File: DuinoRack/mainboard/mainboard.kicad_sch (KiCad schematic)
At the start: 67 parts, among them J1 ISP, J2 SER, J3 Conn_02x08_Odd_Even, J4 Conn_02x05_Odd_Even, J5 Conn_MIDI, U1 MCP4822, U2 ATmega328P-P, U3 TL074, U4 TL431LP, U5 MCP6004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

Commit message: Add programming jumper, fix up MIDI in and THRU
We need to disconnect midi in during programming, since it will pull up
RX. Hence the new jumper.
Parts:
- added C18, C19, C20, C24, C25, C26: 100n, Capacitor_SMD:C_0603_1608Metric_Pad1.08x0.95mm_HandSolder, symbol Device:C
- added C21, C22, C23: 1n, Capacitor_SMD:C_0603_1608Metric_Pad1.08x0.95mm_HandSolder, symbol Device:C
- added H1: MountingHole, MountingHole:MountingHole_3.2mm_M3_DIN965, symbol Mechanical:MountingHole
- added JP1: !PROGRAM, Connector_PinHeader_2.54mm:PinHeader_1x02_P2.54mm_Vertical, symbol Jumper:Jumper_2_Open
- added R29, R36, R37: 220, Resistor_SMD:R_0603_1608Metric_Pad0.98x0.95mm_HandSolder, symbol Device:R
- added R38, R40: 18k, Resistor_SMD:R_0603_1608Metric_Pad0.98x0.95mm_HandSolder, symbol Device:R
- added R39: 4.7k, Resistor_SMD:R_0603_1608Metric_Pad0.98x0.95mm_HandSolder, symbol Device:R
- C2, C4: value C -> 100n
- D7: footprint Diode_SMD:D_SMA-SMB_Universal_Handsoldering -> Diode_SMD:D_SOD-523
- J5: footprint Connector_PinHeader_2.54mm:PinHeader_1x07_P2.54mm_Vertical -> Connector_PinHeader_2.54mm:PinHeader_1x06_P2.54mm_Vertical; symbol Connector:Conn_01x07_Male -> Connector:Conn_01x06_Male
- R27, R28: renamed from R?; footprint (none) -> Resistor_SMD:R_0603_1608Metric_Pad0.98x0.95mm_HandSolder
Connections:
- net +12V: now also C24.1
- net +5V: now also C26.1
- net -12V: now also C25.1
- net GND: now also J3.15 (Pin_15), C18.1, C19.1, C20.1, C22.2, C24.2, C25.2, C26.2, R39.2; no longer J5.1 (Pin_1)
- net MIDI_IN_4: now also J5.1 (Pin_1), R33.2; no longer J5.2 (Pin_2)
- net MIDI_IN_5: now also J5.2 (Pin_2); no longer J5.3 (Pin_3)
- net MIDI_OUT_4: now also J5.5 (Pin_5), R32.2; no longer J5.6 (Pin_6), R31.2
- net MIDI_OUT_5: now also J5.6 (Pin_6), R31.2; no longer J5.7 (Pin_7), R32.2
- net MIDI_THRU_4: now also J5.3 (Pin_3), R26.2; no longer J2.3 (Pin_3), J5.4 (Pin_4), R25.1, U2.2 (PD0), U7.6 (VO2)
- net MIDI_THRU_5: now also J5.4 (Pin_4), R25.1, U7.6 (VO2), JP1.2 (B); no longer J5.5 (Pin_5), R26.2
- net OUTB_INT: now also C23.2, R40.2
- net at U1.6 (VB): now also R29.1
- new net: C19.2, R36.2, R37.1
- new net: C20.2, C21.1, R37.2, R38.1
- new net: C22.1, R38.2, R40.1
- new net: C18.2, R29.2, R36.1
- new net: C21.2, C23.1, R39.1
- new net RX: J2.3 (Pin_3), JP1.1 (A), U2.2 (PD0)
- no-connect marks 3 -> 2
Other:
- note added: "solder jumpers to swap 4/5"
- note removed: "(IN3, inverted)"
- moved on the sheet: C10, C11, C12, C15, C5, C6, C8, C9, D7, R10, R11, R15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

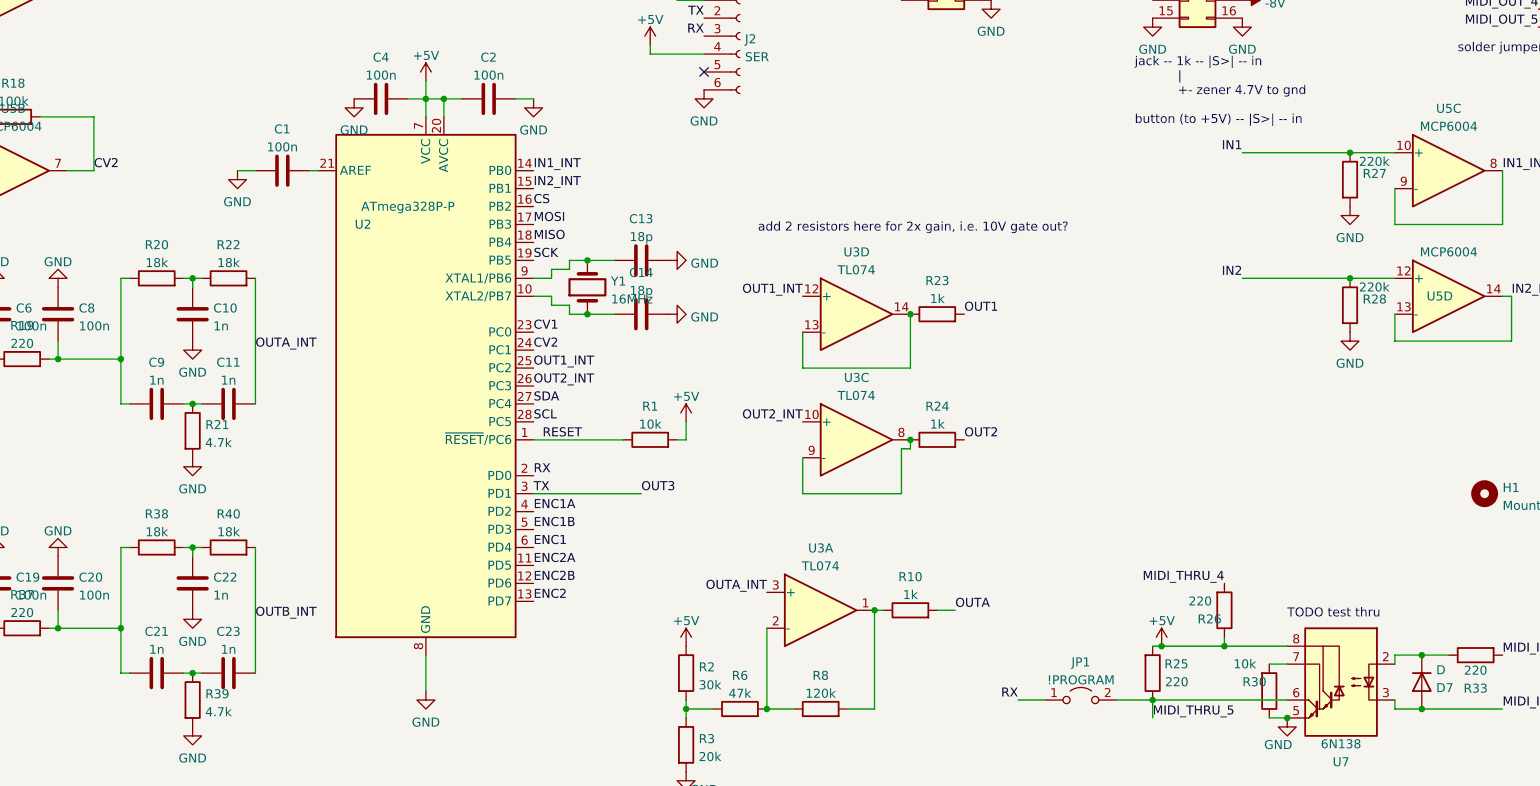
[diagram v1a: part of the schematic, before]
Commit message: Move gate outputs to Timer1 ports
By having the gate outputs connected to Timer1, we can drive them with
PWM, enabling up for other later use cases. A low-pass filter was added
in the output stage to accommodate for this.

We'll keep using normal digital I/O in gate mode, since PWM would be
too noisy there.
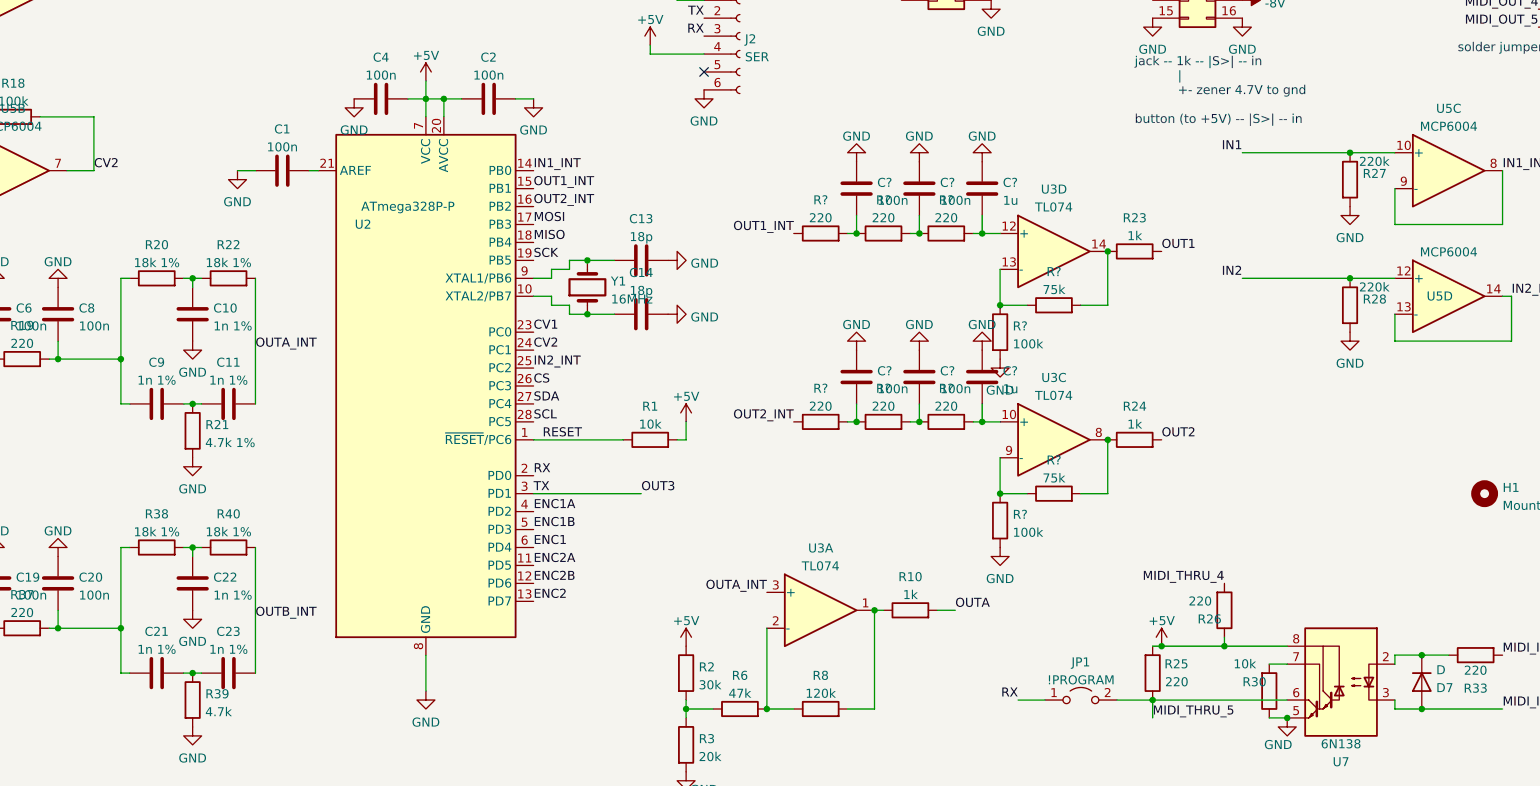
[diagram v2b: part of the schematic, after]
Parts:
- added C? (x4): 100n, Capacitor_SMD:C_0603_1608Metric_Pad1.08x0.95mm_HandSolder, symbol Device:C
- added C? (x2): 1u, Capacitor_SMD:C_0603_1608Metric_Pad1.08x0.95mm_HandSolder, symbol Device:C
- added R? (x2): 75k, symbol Device:R
- added R? (x6): 220, Resistor_SMD:R_0603_1608Metric_Pad0.98x0.95mm_HandSolder, symbol Device:R
- added R? (x2): 100k, symbol Device:R
- C10, C11, C21, C22, C23, C9: value 1n -> 1n 1%
- R20, R22, R38, R40: value 18k -> 18k 1%
- R21: value 4.7k -> 4.7k 1%
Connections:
- net CS: now also U2.26 (PC3); no longer U2.16 (PB2)
- net GND: now also C?.1, C?.1, C?.1, C?.1, C?.1, C?.1, R?.2, R?.2
- net IN2_INT: now also U2.25 (PC2); no longer U2.15 (PB1)
- net OUT1_INT: now also U2.15 (PB1), R?.1; no longer U2.25 (PC2), U3.12 (+)
- net OUT2_INT: now also U2.16 (PB2), R?.1; no longer U2.26 (PC3), U3.10 (+)
- net at R23.1, U3.14: now also R?.2; no longer U3.13 (-)
- net at R24.1, U3.8: now also R?.2; no longer U3.9 (-)
- new net: R?.1, R?.1, U3.13 (-)
- new net: C?.2, R?.1, R?.2 (x4)
- new net: C?.2, R?.2, U3.12 (+)
- new net: R?.1, R?.1, U3.9 (-)
- new net: C?.2, R?.2, U3.10 (+)
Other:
- note removed: "TODO test thru"
- note removed: "add 2 resistors here for 2x gain, i.e. 10V gate out?"
- moved on the sheet: R23, R24, U3C, U3D

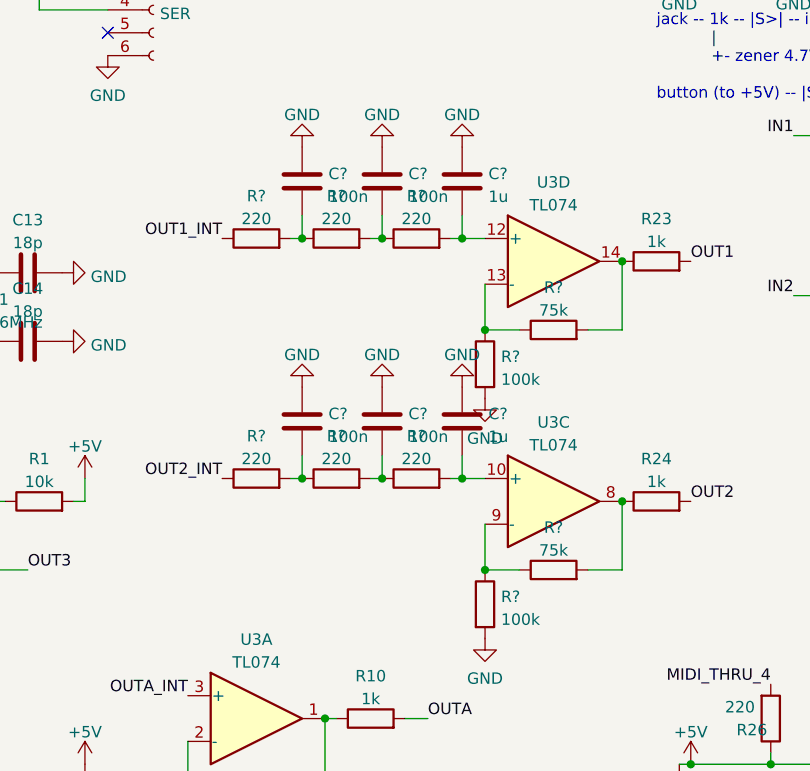
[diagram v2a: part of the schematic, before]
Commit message: Update layout with latest pcb changes
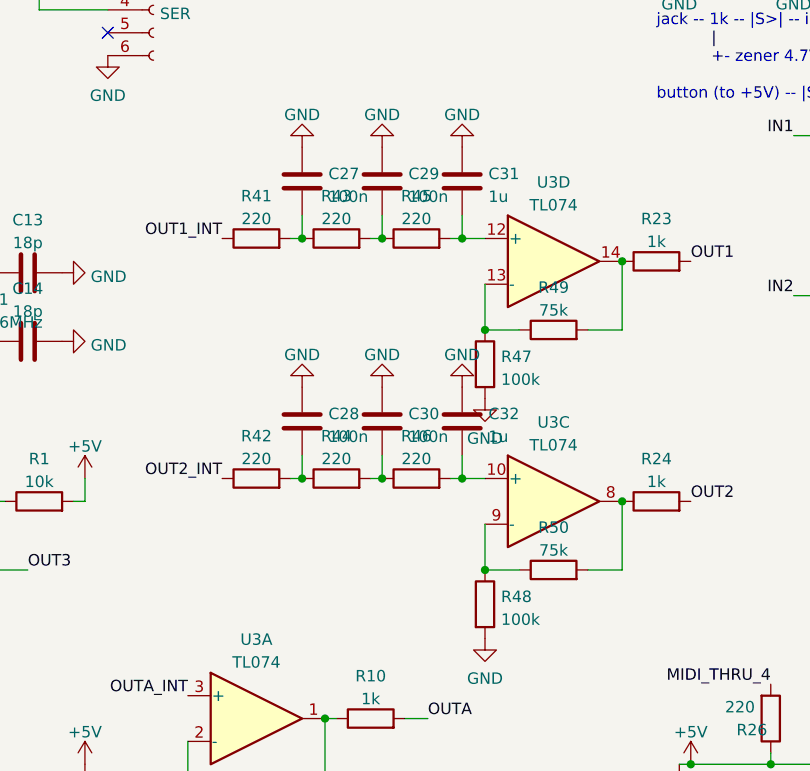
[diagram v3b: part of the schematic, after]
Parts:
- R47, R48, R49, R50: renamed from R?; footprint (none) -> Resistor_SMD:R_0603_1608Metric_Pad0.98x0.95mm_HandSolder
- gave numbers to parts that had none: 12

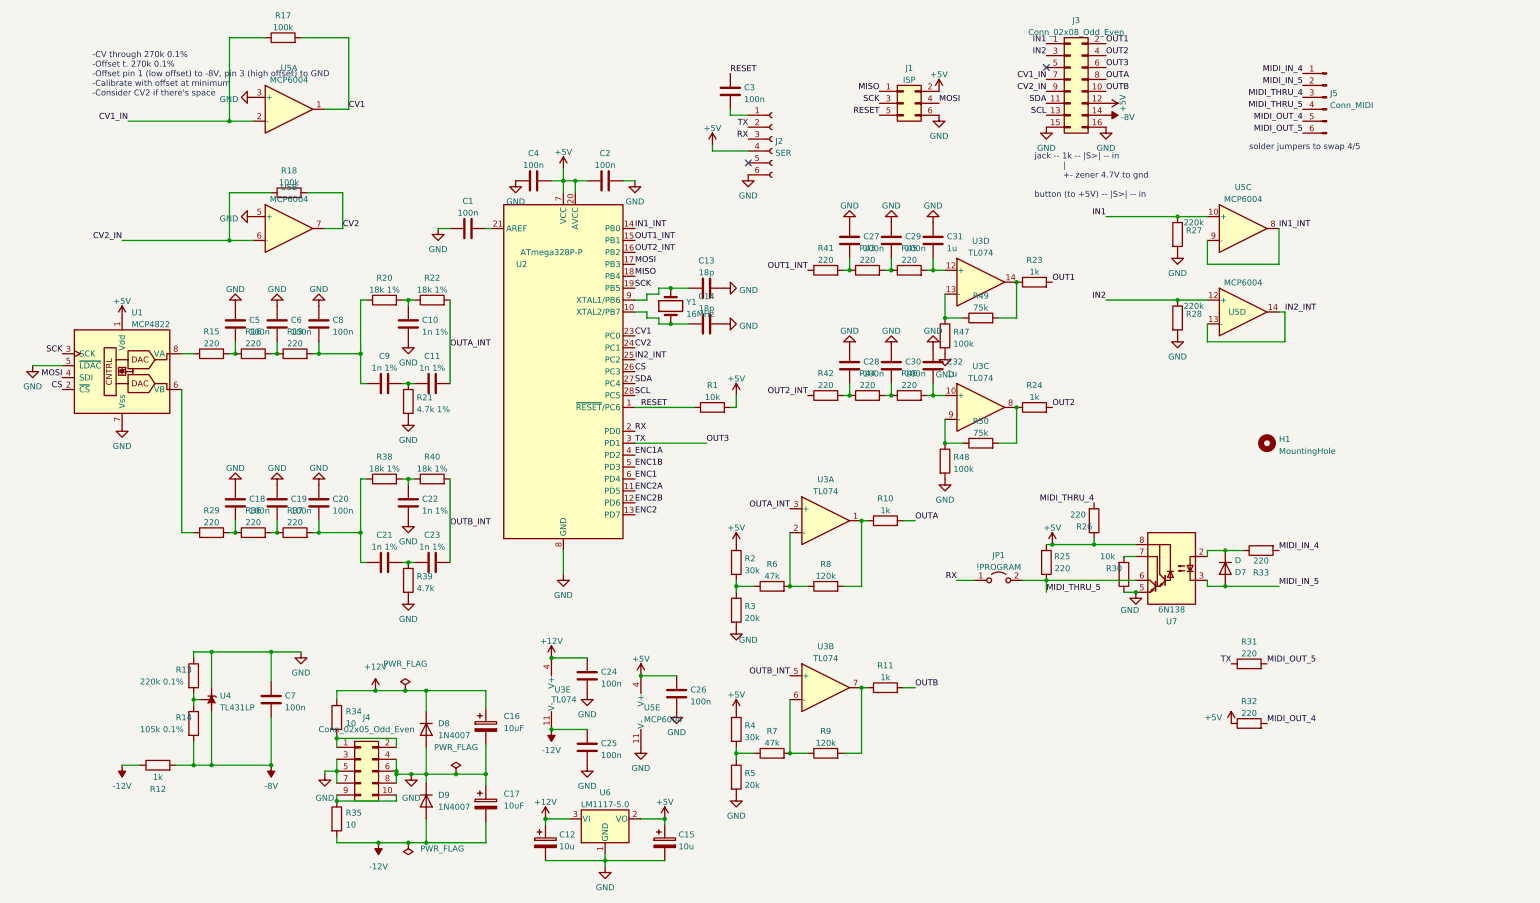
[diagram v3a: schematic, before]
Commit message: Add configurable input protection to enable gate IN3
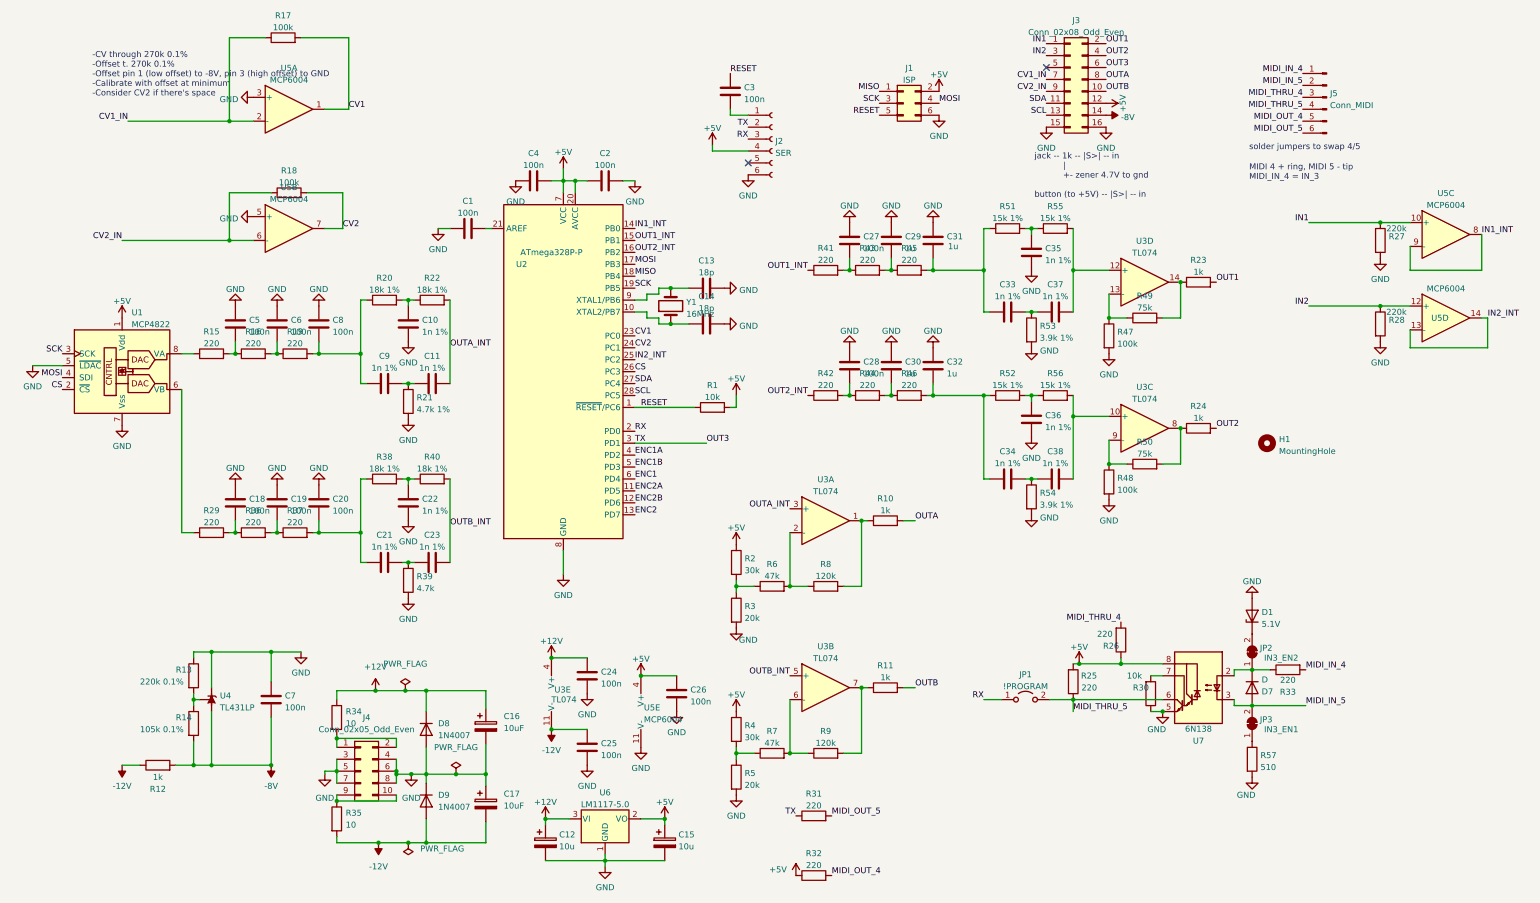
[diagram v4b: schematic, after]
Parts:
- added C33, C34, C35, C36, C37, C38: 1n 1%, Capacitor_SMD:C_0603_1608Metric_Pad1.08x0.95mm_HandSolder, symbol Device:C
- added D1: 5.1V, Diode_THT:D_DO-35_SOD27_P2.54mm_Vertical_AnodeUp, symbol Device:D_Zener
- added JP2: IN3_EN2, Jumper:SolderJumper-2_P1.3mm_Bridged_RoundedPad1.0x1.5mm, symbol Jumper:SolderJumper_2_Bridged
- added JP3: IN3_EN1, Jumper:SolderJumper-2_P1.3mm_Bridged_RoundedPad1.0x1.5mm, symbol Jumper:SolderJumper_2_Bridged
- added R51, R52, R55, R56: 15k 1%, Resistor_SMD:R_0603_1608Metric_Pad0.98x0.95mm_HandSolder, symbol Device:R
- added R53, R54: 3.9k 1%, Resistor_SMD:R_0603_1608Metric_Pad0.98x0.95mm_HandSolder, symbol Device:R
- added R57: 510, Resistor_SMD:R_0603_1608Metric_Pad0.98x0.95mm_HandSolder, symbol Device:R
- C29, C30: value 100n -> 1u
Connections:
- net GND: now also C35.2, C36.2, D1.2 (A), R53.2, R54.2, R57.2
- net MIDI_IN_5: now also JP3.2 (B)
- net at C31.2, R45.2: now also C33.1, R51.1; no longer U3.12 (+)
- net at D7.1 (K), R33.1, U7.2 (C1): now also JP2.1 (A)
- net at C32.2, R46.2: now also C34.1, R52.1; no longer U3.10 (+)
- new net: C37.2, R55.2, U3.12 (+)
- new net: C33.2, C37.1, R53.1
- new net: C34.2, C38.1, R54.1
- new net: C35.1, R51.2, R55.1
- new net: D1.1 (K), JP2.2 (B)
- new net: JP3.1 (A), R57.1
- new net: C38.2, R56.2, U3.10 (+)
- new net: C36.1, R52.2, R56.1
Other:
- note added: "MIDI 4 + ring, MIDI 5 - tip MIDI_IN_4 = IN_3"
- moved on the sheet: D7, JP1, R23, R24, R25, R26, R27, R28, R30, R31, R32, R33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

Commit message: Finish DuinoRack hardware, final touches on AS3340 VCO
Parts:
- removed J1: ISP, Connector_PinHeader_2.54mm:PinHeader_2x03_P2.54mm_Vertical, symbol Connector_Generic:Conn_02x03_Odd_Even
- removed U4: TL431LP, Package_TO_SOT_THT:TO-92_Inline, symbol Reference_Voltage:TL431LP
- added C39, C40: 100n, Capacitor_SMD:C_0603_1608Metric_Pad1.08x0.95mm_HandSolder, symbol Device:C
- added J6: Conn_02x03_Odd_Even, Connector_PinHeader_2.54mm:PinHeader_2x03_P2.54mm_Vertical, symbol Connector_Generic:Conn_02x03_Odd_Even
- added R58: 330, Resistor_SMD:R_0603_1608Metric_Pad0.98x0.95mm_HandSolder, symbol Device:R
- added R59, R60: 100k 0.1%, Resistor_SMD:R_0603_1608Metric_Pad0.98x0.95mm_HandSolder, symbol Device:R
- added U4, U8: TL431DBZ, Package_TO_SOT_SMD:SOT-23, symbol Reference_Voltage:TL431DBZ
- D7: value D -> 1N4148WS; footprint Diode_SMD:D_SOD-523 -> Diode_SMD:D_SOD-323_HandSoldering
- R13: value 220k 0.1% -> 200k 0.1%
- R14: value 105k 0.1% -> 100k 0.1%
- R51, R52, R55, R56: value 15k 1% -> 15k 0.1%
- R53, R54: value 3.9k 1% -> 3.9k 0.1%
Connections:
- net +12V: now also J3.16 (Pin_16), R58.1
- net +5V: now also J2.3 (Pin_3); no longer C2.1, J2.4 (Pin_4), U1.1 (Vdd), U2.20 (AVCC)
- net -8V: now also U4.3 (A)
- net ENC1: now also J6.6 (Pin_6)
- net ENC1A: now also J6.2 (Pin_2)
- net ENC1B: now also J6.4 (Pin_4)
- net ENC2: now also J6.5 (Pin_5)
- net ENC2A: now also J6.1 (Pin_1)
- net ENC2B: now also J6.3 (Pin_3)
- net GND: now also C39.1, C40.2, R60.2, U4.1 (K), U8.3 (A); no longer J3.16 (Pin_16)
- net OUT3: now also J2.5 (Pin_5); no longer J2.2 (Pin_2)
- net RX: now also J2.4 (Pin_4); no longer J2.3 (Pin_3)
- net at R13.2, R14.1: now also U4.2 (REF)
- new net: R59.2, R60.1, U8.2 (REF)
- new net +5VA: C2.1, C39.2, C40.1, R58.2, R59.1, U1.1 (Vdd), U2.20 (AVCC), U8.1 (K)
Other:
- moved on the sheet: C7, R12, R13, R14
